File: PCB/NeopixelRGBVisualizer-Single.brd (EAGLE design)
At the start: 55 x 30 mm, 24 parts, among them CN2 5-12VDC, IC1 MSGEQ7, IC2 78L05ACZ-AP, Q1 16MHz, X1 STEREOJACK

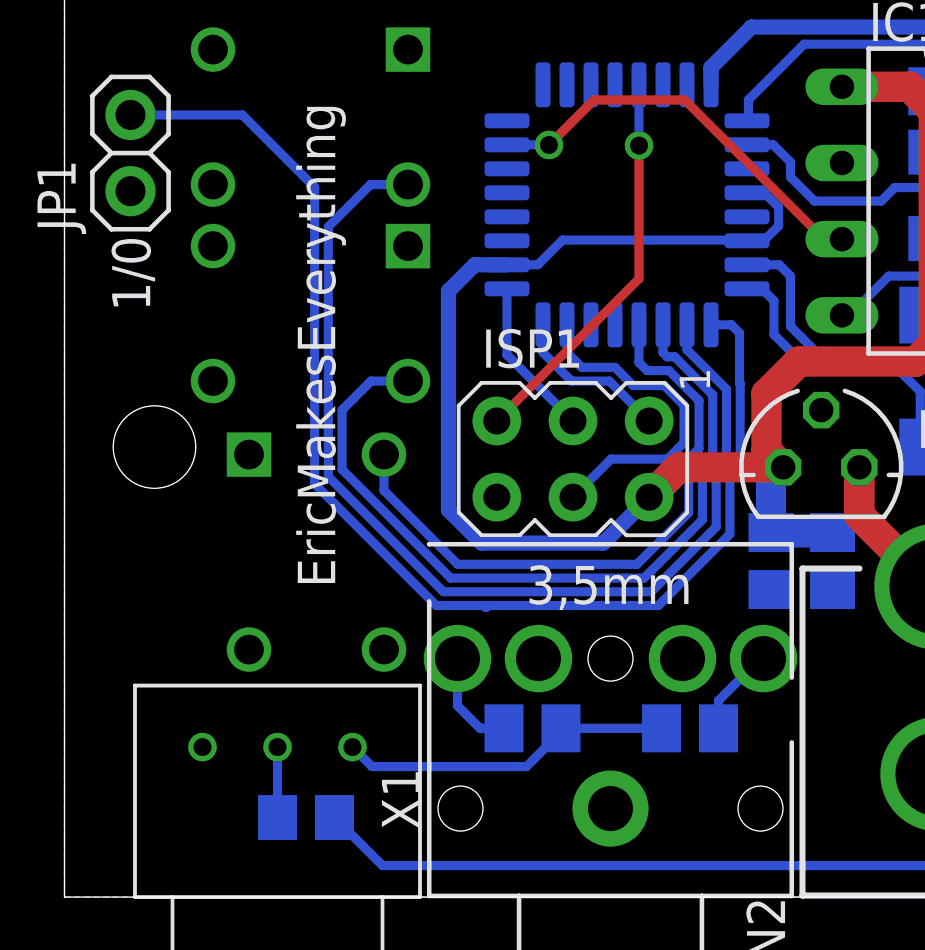
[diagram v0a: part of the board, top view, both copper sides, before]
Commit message: Updated board to have correct footprints for tactile switches and potentiometer, since footprints acquired from SnapEDA were wrong.
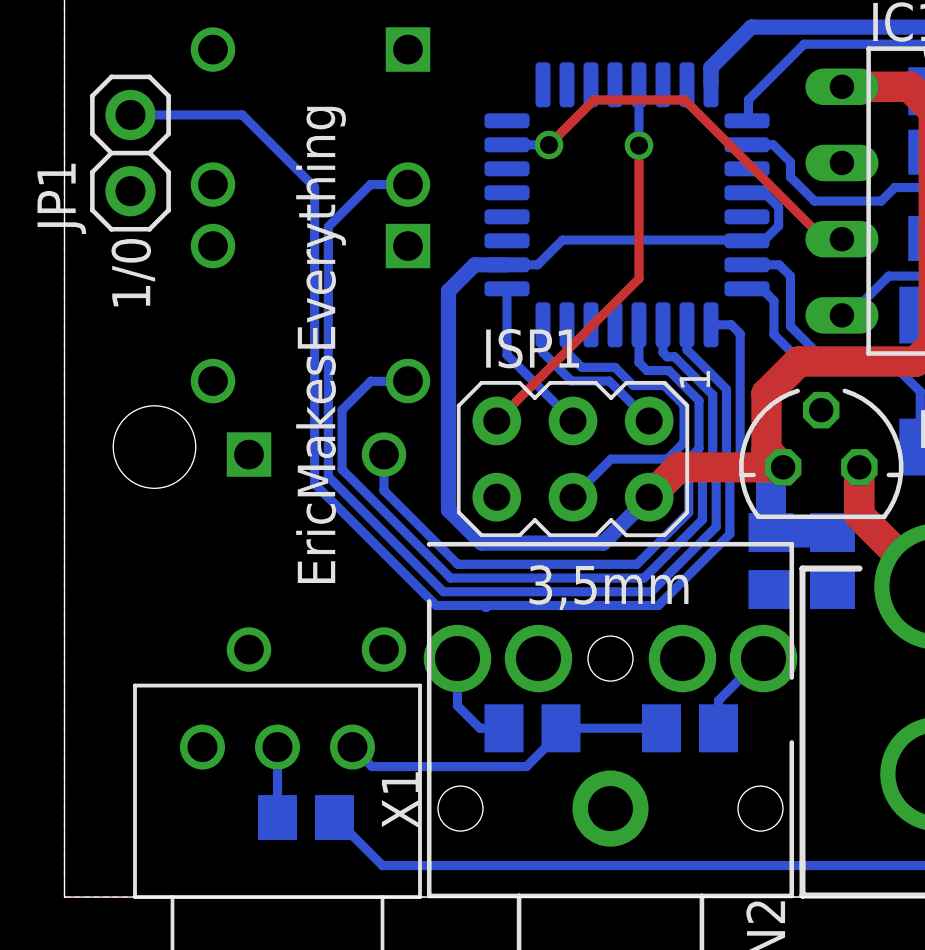
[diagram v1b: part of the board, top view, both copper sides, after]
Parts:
- C7: value 0.1u -> 0.33u
- C8: value 0.33u -> 0.1u
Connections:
- net GND: now also S1.1, S2.1, S3.1; no longer S1.4, S2.4, S3.4
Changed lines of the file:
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@@
 <drawing>
 <settings>
-<setting alwaysvectorfont="yes"/>
+<setting alwaysvectorfont="no"/>
 <setting keepoldvectorfont="yes"/>
 <setting verticaltext="up"/>
 </settings>
-<grid distance="0.1" unitdist="mm" unit="mm" style="lines" multiple="1" display="yes" altdistance="0.1" altunitdist="mm" altunit="mm"/>
+<grid distance="1" unitdist="mm" unit="mm" style="lines" multiple="1" display="yes" altdistance="0.1" altunitdist="mm" altunit="mm"/>
 <layers>
-<layer number="1" name="Top" color="4" fill="1" visible="yes" active="yes"/>
+<layer number="1" name="Top" color="4" fill="1" visible="no" active="yes"/>
 <layer number="16" name="Bottom" color="1" fill="1" visible="yes" active="yes"/>
 <layer number="17" name="Pads" color="2" fill="1" visible="yes" active="yes"/>
@@
 <layer number="19" name="Unrouted" color="6" fill="1" visible="yes" active="yes"/>
 <layer number="20" name="Dimension" color="15" fill="1" visible="yes" active="yes"/>
-<layer number="21" name="tPlace" color="7" fill="1" visible="yes" active="yes"/>
+<layer number="21" name="tPlace" color="7" fill="1" visible="no" active="yes"/>
 <layer number="22" name="bPlace" color="7" fill="1" visible="yes" active="yes"/>
-<layer number="23" name="tOrigins" color="15" fill="1" visible="yes" active="yes"/>
+<layer number="23" name="tOrigins" color="15" fill="1" visible="no" active="yes"/>
 <layer number="24" name="bOrigins" color="15" fill="1" visible="yes" active="yes"/>
-<layer number="25" name="tNames" color="7" fill="1" visible="yes" active="yes"/>
+<layer number="25" name="tNames" color="7" fill="1" visible="no" active="yes"/>
 <layer number="26" name="bNames" color="7" fill="1" visible="yes" active="yes"/>
-<layer number="27" name="tValues" color="7" fill="1" visible="yes" active="yes"/>
+<layer number="27" name="tValues" color="7" fill="1" visible="no" active="yes"/>
 <layer number="28" name="bValues" color="7" fill="1" visible="yes" active="yes"/>
-<layer number="29" name="tStop" color="7" fill="3" visible="yes" active="yes"/>
+<layer number="29" name="tStop" color="7" fill="3" visible="no" active="yes"/>
 <layer number="30" name="bStop" color="7" fill="6" visible="yes" active="yes"/>
 <layer number="31" name="tCream" color="7" fill="4" visible="no" active="yes"/>
@@
 <layer number="49" name="Reference" color="7" fill="1" visible="no" active="yes"/>
 <layer number="50" name="dxf" color="7" fill="1" visible="no" active="no"/>
-<layer number="51" name="tDocu" color="7" fill="1" visible="yes" active="yes"/>
+<layer number="51" name="tDocu" color="7" fill="1" visible="no" active="yes"/>
 <layer number="52" name="bDocu" color="7" fill="1" visible="yes" active="yes"/>
 <layer number="53" name="tGND_GNDA" color="7" fill="9" visible="no" active="no"/>
@@
 <attribute name="SPICEPREFIX" value="C" x="32.775" y="15.2" size="1.778" layer="28" rot="MR90" display="off"/>
 </element>
-<element name="C7" library="rcl" library_urn="urn:adsk.eagle:library:334" package="C0805" package3d_urn="urn:adsk.eagle:package:23617/2" value="0.1u" x="25.6" y="11.2" rot="MR270">
+<element name="C7" library="rcl" library_urn="urn:adsk.eagle:library:334" package="C0805" package3d_urn="urn:adsk.eagle:package:23617/2" value="0.33u" x="25.6" y="11.2" rot="MR270">
 <attribute name="NAME" x="25.6" y="8.2" size="1" layer="26" font="vector" rot="SMR90" align="center"/>
 <attribute name="SPICEPREFIX" value="C" x="25.6" y="11.2" size="1.778" layer="28" rot="MR270" display="off"/>
@@
 <element name="U$1" library="ATMega" package="32M1-A" value="ATMEGA328-TQFP" x="18.75" y="23.075" rot="MR0"/>
 <element name="X1" library="adafruit" package="STX3100" value="STEREOJACK" x="18.1" y="0.25" rot="R90"/>
-<element name="C8" library="rcl" library_urn="urn:adsk.eagle:library:334" package="C0805" package3d_urn="urn:adsk.eagle:package:23617/2" value="0.33u" x="33.775" y="12.15" rot="MR180">
+<element name="C8" library="rcl" library_urn="urn:adsk.eagle:library:334" package="C0805" package3d_urn="urn:adsk.eagle:package:23617/2" value="0.1u" x="33.775" y="12.15" rot="MR180">
 <attribute name="NAME" x="36.1" y="12.1" size="1" layer="26" font="vector" rot="MR90" align="center"/>
 <attribute name="SPICEPREFIX" value="C" x="33.775" y="12.15" size="1.778" layer="28" rot="MR180" display="off"/>
@@
 <contactref element="IC2" pad="GND"/>
 <contactref element="U$2" pad="P$1"/>
-<contactref element="S3" pad="4"/>
-<contactref element="S1" pad="3"/>
-<contactref element="S1" pad="4"/>
-<contactref element="S2" pad="3"/>
-<contactref element="S2" pad="4"/>
-<contactref element="S3" pad="3"/>
 <contactref element="U$3" pad="P$3"/>
 <contactref element="CN2" pad="GNDBREAK"/>
 <contactref element="JP1" pad="1"/>
+<contactref element="S1" pad="1"/>
+<contactref element="S2" pad="1"/>
+<contactref element="S3" pad="1"/>
+<contactref element="S1" pad="3"/>
+<contactref element="S2" pad="3"/>
+<contactref element="S3" pad="3"/>
 </signal>
 <signal name="N$6">
@@
 </signal>
 <signal name="N$18">
-<contactref element="S1" pad="2"/>
 <contactref element="U$1" pad="12"/>
 <wire x1="20.15" y1="17.55" x2="19.41716875" y2="17.55" width="0.3048" layer="16"/>
@@
 <wire x1="21.15" y1="16.55" x2="20.15" y2="17.55" width="0.3048" layer="16"/>
 <wire x1="19.08173125" y1="11.0912" x2="13.1088" y2="11.0912" width="0.3048" layer="16"/>
-<wire x1="10.65" y1="14.75" x2="10.65" y2="13.55" width="0.3048" layer="16"/>
 <wire x1="13.1088" y1="11.0912" x2="10.65" y2="13.55" width="0.3048" layer="16"/>
 <wire x1="21.15" y1="16.55" x2="21.15" y2="14.95" width="0.3048" layer="16"/>
@@
 <wire x1="20.8076" y1="12.81706875" x2="19.08173125" y2="11.0912" width="0.3048" layer="16"/>
 <wire x1="21.15" y1="14.95" x2="20.8076" y2="14.6076" width="0.3048" layer="16"/>
+<contactref element="S1" pad="2"/>
+<wire x1="10.65" y1="13.55" x2="10.65" y2="14.75" width="0.3048" layer="16"/>
 </signal>
 <signal name="N$19">
 <contactref element="U$1" pad="10"/>
-<contactref element="S3" pad="2"/>
 <wire x1="19.56049375" y1="10.1768" x2="12.6300375" y2="10.1768" width="0.3048" layer="16"/>
 <wire x1="12.6300375" y1="10.1768" x2="8.7955" y2="14.0113375" width="0.3048" layer="16"/>
 <wire x1="20.75" y1="19.075" x2="20.75" y2="18.2431625" width="0.3048" layer="16"/>
 <wire x1="22.0644" y1="16.9287625" x2="20.75" y2="18.2431625" width="0.3048" layer="16"/>
-<wire x1="11.45" y1="23.75" x2="10.2" y2="23.75" width="0.3048" layer="16"/>
 <wire x1="8.7955" y1="22.3455" x2="8.7955" y2="14.0113375" width="0.3048" layer="16"/>
-<wire x1="10.2" y1="23.75" x2="8.7955" y2="22.3455" width="0.3048" layer="16"/>
+<wire x1="8.7955" y1="22.3455" x2="10.2" y2="23.75" width="0.3048" layer="16"/>
 <wire x1="22.0644" y1="16.9287625" x2="22.0644" y2="14.5712375" width="0.3048" layer="16"/>
 <wire x1="22.0644" y1="14.5712375" x2="21.722" y2="14.2288375" width="0.3048" layer="16"/>
 <wire x1="21.722" y1="12.33830625" x2="19.56049375" y2="10.1768" width="0.3048" layer="16"/>
 <wire x1="21.722" y1="14.2288375" x2="21.722" y2="12.33830625" width="0.3048" layer="16"/>
+<contactref element="S3" pad="2"/>
+<wire x1="10.2" y1="23.75" x2="11.45" y2="23.75" width="0.3048" layer="16"/>
 </signal>
 <signal name="N$20">
@@
 <contactref element="JP1" pad="2"/>
 <wire x1="22.225" y1="19.075" x2="21.55" y2="19.075" width="0.3048" layer="16"/>
-<wire x1="22.5" y1="18.8" x2="22.225" y2="19.075" width="0.3048" layer="16"/>
+<wire x1="22.5216" y1="18.7784" x2="22.225" y2="19.075" width="0.3048" layer="16"/>
 <wire x1="22.1792" y1="14.03945625" x2="22.1792" y2="12.098925" width="0.3048" layer="16"/>
 <wire x1="14.1196" y1="9.7196" x2="14.05" y2="9.65" width="0.3048" layer="16"/>
-<wire x1="22.5216" y1="17.11814375" x2="22.5216" y2="14.38185625" width="0.3048" layer="16"/>
 <wire x1="22.5216" y1="14.38185625" x2="22.1792" y2="14.03945625" width="0.3048" layer="16"/>
 <wire x1="22.1792" y1="12.098925" x2="19.799875" y2="9.7196" width="0.3048" layer="16"/>
 <wire x1="19.799875" y1="9.7196" x2="14.1196" y2="9.7196" width="0.3048" layer="16"/>
-<wire x1="22.5216" y1="17.11814375" x2="22.5" y2="17.13974375" width="0.3048" layer="16"/>
-<wire x1="22.5" y1="18.8" x2="22.5" y2="17.13974375" width="0.3048" layer="16"/>
+<wire x1="22.5216" y1="18.7784" x2="22.5216" y2="14.38185625" width="0.3048" layer="16"/>
 <wire x1="14.05" y1="9.65" x2="13.9804" y2="9.7196" width="0.3048" layer="16"/>
 <wire x1="13.9804" y1="9.7196" x2="12.39065625" y2="9.7196" width="0.3048" layer="16"/>
@@
 <signal name="N$8">
 <contactref element="U$1" pad="11"/>
-<contactref element="S2" pad="2"/>
 <wire x1="19.95" y1="19.075" x2="19.95" y2="18.15" width="0.3048" layer="16"/>
 <wire x1="20.0928" y1="18.0072" x2="19.95" y2="18.15" width="0.3048" layer="16"/>
@@
 <wire x1="12.86941875" y1="10.634" x2="9.2527" y2="14.25071875" width="0.3048" layer="16"/>
 <wire x1="9.2527" y1="16.23380625" x2="9.2527" y2="14.25071875" width="0.3048" layer="16"/>
-<wire x1="11.45" y1="17.2" x2="10.21889375" y2="17.2" width="0.3048" layer="16"/>
-<wire x1="10.21889375" y1="17.2" x2="9.2527" y2="16.23380625" width="0.3048" layer="16"/>
+<wire x1="10.21889375" y1="17.2" x2="10.209446875" y2="17.190553125" width="0.3048" layer="16"/>
+<wire x1="10.209446875" y1="17.190553125" x2="9.2527" y2="16.23380625" width="0.3048" layer="16"/>
 <wire x1="21.6072" y1="16.73938125" x2="20.33938125" y2="18.0072" width="0.3048" layer="16"/>
 <wire x1="21.6072" y1="16.73938125" x2="21.6072" y2="14.76061875" width="0.3048" layer="16"/>
@@
 <wire x1="21.2648" y1="12.5776875" x2="19.3211125" y2="10.634" width="0.3048" layer="16"/>
 <wire x1="21.2648" y1="14.41821875" x2="21.2648" y2="12.5776875" width="0.3048" layer="16"/>
+<wire x1="10.209446875" y1="17.190553125" x2="11.440553125" y2="17.190553125" width="0.3048" layer="16"/>
+<contactref element="S2" pad="2"/>
+<wire x1="11.440553125" y1="17.190553125" x2="11.45" y2="17.2" width="0" layer="19" extent="16-16"/>
 </signal>
 </signals>

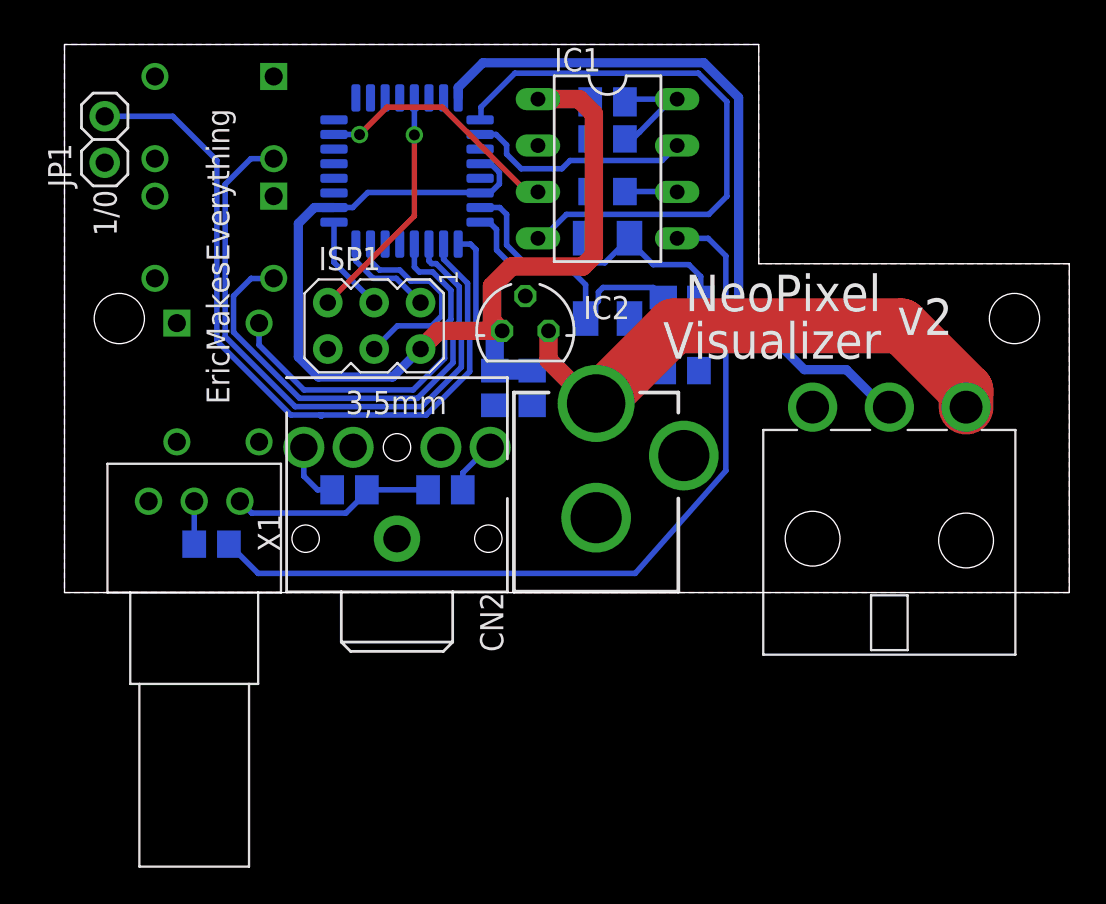
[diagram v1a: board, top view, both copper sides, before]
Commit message: Found problem in proto2 board to be caused by knockoff MSGEQ7 chip. Maintained fixed pinouts of tactile switches and removed potentiometer from board.  Electrically, that circuit did not serve its purpose, and testing with multiple devices shows that the recommended configuration of the MSGEQ7 is fine for most consumer electronics.  Post-input gain processing will have to be managed with the tactile buttons. Added 1.5mm holes centered under each of the tactile buttons to locate pilot holes.
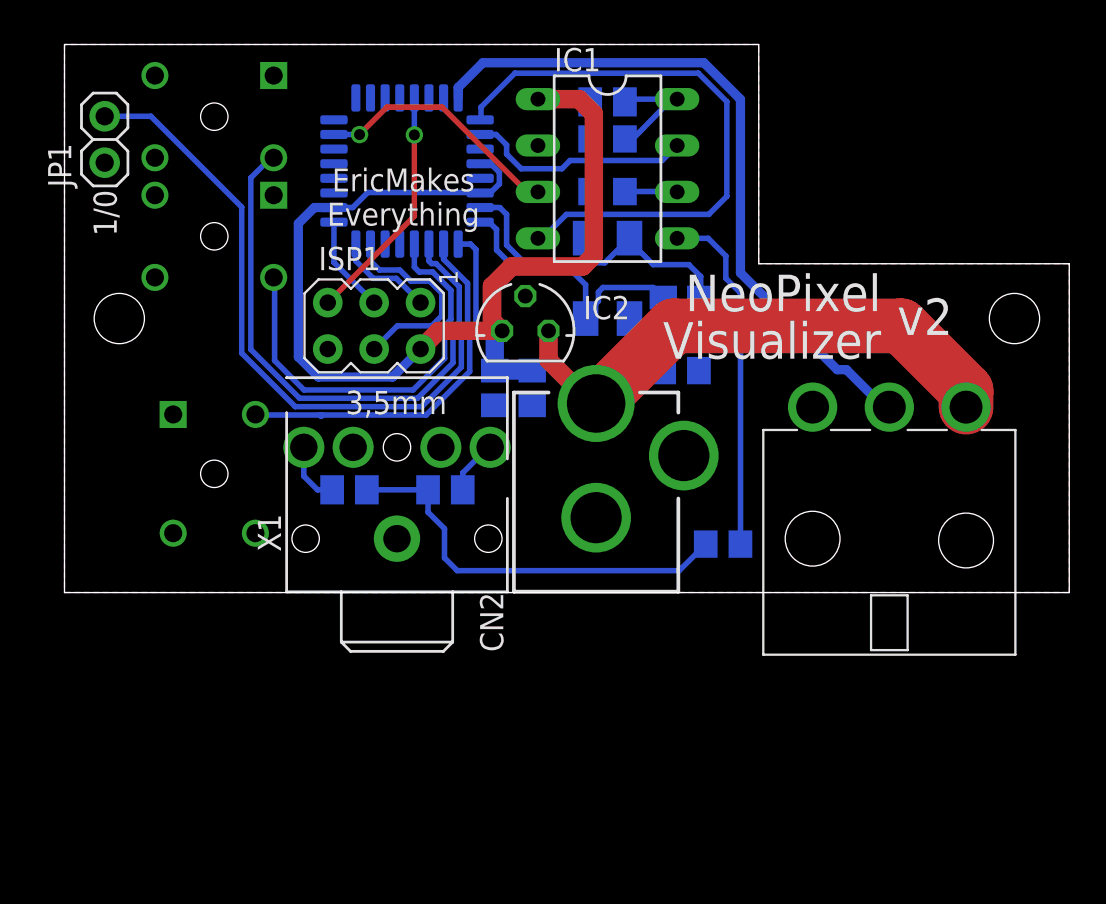
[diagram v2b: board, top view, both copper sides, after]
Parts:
- removed U$2: PTD901-2015K, potentiometers:PTD901-2015K-####
- moved C1 28.0 mm to (36.0, 2.65)
- moved S1 5.00 mm to (8.20, 6.50)
- moved S2 0.05 mm to (8.20, 19.5)
- moved S3 0.05 mm to (8.20, 26.1)
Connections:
- removed net N$6: R1.1, R2.1, U$2.P$3
- net GND: no longer U$2.P$1
- net N$16: now also R1.1, R2.1; no longer U$2.P$2
- net N$18: now also S2.2; no longer S1.2
- net N$19: now also JP1.2; no longer S3.2
- net N$20: now also S1.2; no longer JP1.2
- net N$8: now also S3.2; no longer S2.2
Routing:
- net N$10: track 45.2 -> 19.2 mm
- net N$20: track 41.5 -> 20.7 mm
- net N$16: track 2.35 -> 22.6 mm
- net N$6: track 11.2 -> 0.00 mm
- net N$8: track 26.4 -> 31.5 mm
- net N$19: track 34.4 -> 39.1 mm
- net N$18: track 20.7 -> 22.9 mm
- net N$17: track 39.2 -> 38.1 mm
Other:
- board text added: "EricMakes Everything"
- board text removed: "EricMakesEverything"

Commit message: Added headers to access serial TX/RX pins, power, and GND.  Requried 2 more vias.
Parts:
- added JP2: (no value), mypinhead:1X04-OCT
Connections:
- new net RX: JP2.3, U$1.30
- new net TX: JP2.2, U$1.31
- net GND: now also JP2.4
- net VCC: now also JP2.1
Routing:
- net TX: track 0.00 -> 35.7 mm, vias 0 -> 1
- net RX: track 0.00 -> 32.6 mm, vias 0 -> 1
- net VCC: track 61.2 -> 82.6 mm
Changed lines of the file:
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@@
 <attribute name="VALUE" x="2.225" y="22.04" size="1.27" layer="25" font="vector" rot="R270" align="center-left"/>
+</element>
+<element name="JP2" library="mypinhead" package="1X04-OCT" value="" x="2.2" y="7.2" rot="R90">
+<attribute name="NAME" x="0.3712" y="2.0438" size="1.27" layer="25" ratio="10" rot="R90"/>
+<attribute name="VALUE" x="5.375" y="2.12" size="1.27" layer="27" rot="R90"/>
 </element>
 </elements>
@@
 <contactref element="S1" pad="1"/>
 <contactref element="S1" pad="3"/>
+<contactref element="JP2" pad="4"/>
 </signal>
 <signal name="N$10">
@@
 <wire x1="17.96" y1="11.8" x2="13.9" y2="11.8" width="0.508" layer="16"/>
 <wire x1="19.49" y1="13.33" x2="17.96" y2="11.8" width="0.508" layer="16"/>
+<contactref element="JP2" pad="1"/>
+<wire x1="10.61" y1="11.8" x2="2.2" y2="3.39" width="0.3048" layer="1"/>
+<wire x1="17.96" y1="11.8" x2="19.49" y2="13.33" width="0.3048" layer="1"/>
+<wire x1="10.61" y1="11.8" x2="17.96" y2="11.8" width="0.3048" layer="1"/>
 </signal>
 <signal name="N$16">
@@
 <wire x1="11.3" y1="23.8" x2="10.2" y2="22.7" width="0.3048" layer="16"/>
 </signal>
+<signal name="TX">
+<contactref element="U$1" pad="31"/>
+<contactref element="JP2" pad="2"/>
+<wire x1="20.75" y1="28.5" x2="17.15" y2="28.5" width="0.3048" layer="1"/>
+<via x="20.75" y="28.5" extent="1-16" drill="0.35"/>
+<wire x1="20.75" y1="28.5" x2="20.75" y2="27.075" width="0.3048" layer="16"/>
+<wire x1="14.9" y1="26.25" x2="17.15" y2="28.5" width="0.3048" layer="1"/>
+<wire x1="10.1572" y1="24.85" x2="11.55" y2="26.2428" width="0.3048" layer="1"/>
+<wire x1="11.55" y1="26.2428" x2="13.88938125" y2="26.2428" width="0.3048" layer="1"/>
+<wire x1="13.88938125" y1="26.2428" x2="13.89658125" y2="26.25" width="0.3048" layer="1"/>
+<wire x1="13.89658125" y1="26.25" x2="14.9" y2="26.25" width="0.3048" layer="1"/>
+<wire x1="4.4072" y1="8.1372" x2="2.2" y2="5.93" width="0.3048" layer="1"/>
+<wire x1="4.4072" y1="8.1372" x2="4.4072" y2="12.38061875" width="0.3048" layer="1"/>
+<wire x1="10.1572" y1="18.13061875" x2="10.1572" y2="24.85" width="0.3048" layer="1"/>
+<wire x1="4.4072" y1="12.38061875" x2="10.1572" y2="18.13061875" width="0.3048" layer="1"/>
+</signal>
+<signal name="RX">
+<contactref element="U$1" pad="30"/>
+<contactref element="JP2" pad="3"/>
+<wire x1="19.95" y1="27.075" x2="19.95" y2="28.05" width="0.3048" layer="16"/>
+<wire x1="19.5" y1="28.5" x2="14.45" y2="28.5" width="0.3048" layer="16"/>
+<via x="14.45" y="28.5" extent="1-16" drill="0.35"/>
+<wire x1="14.45" y1="28.5" x2="12.65" y2="26.7" width="0.3048" layer="1"/>
+<wire x1="3.95" y1="10.22" x2="3.95" y2="12.57" width="0.3048" layer="1"/>
+<wire x1="3.95" y1="10.22" x2="2.2" y2="8.47" width="0.3048" layer="1"/>
+<wire x1="19.95" y1="28.05" x2="19.5" y2="28.5" width="0.3048" layer="16"/>
+<wire x1="9.7" y1="18.32" x2="3.95" y2="12.57" width="0.3048" layer="1"/>
+<wire x1="11.15" y1="26.7" x2="9.7" y2="25.25" width="0.3048" layer="1"/>
+<wire x1="11.15" y1="26.7" x2="12.65" y2="26.7" width="0.3048" layer="1"/>
+<wire x1="9.7" y1="18.32" x2="9.7" y2="25.25" width="0.3048" layer="1"/>
+</signal>
 </signals>
